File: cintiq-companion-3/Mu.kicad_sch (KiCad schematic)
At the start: 12 parts, among them J1 Conn_01x03_Pin

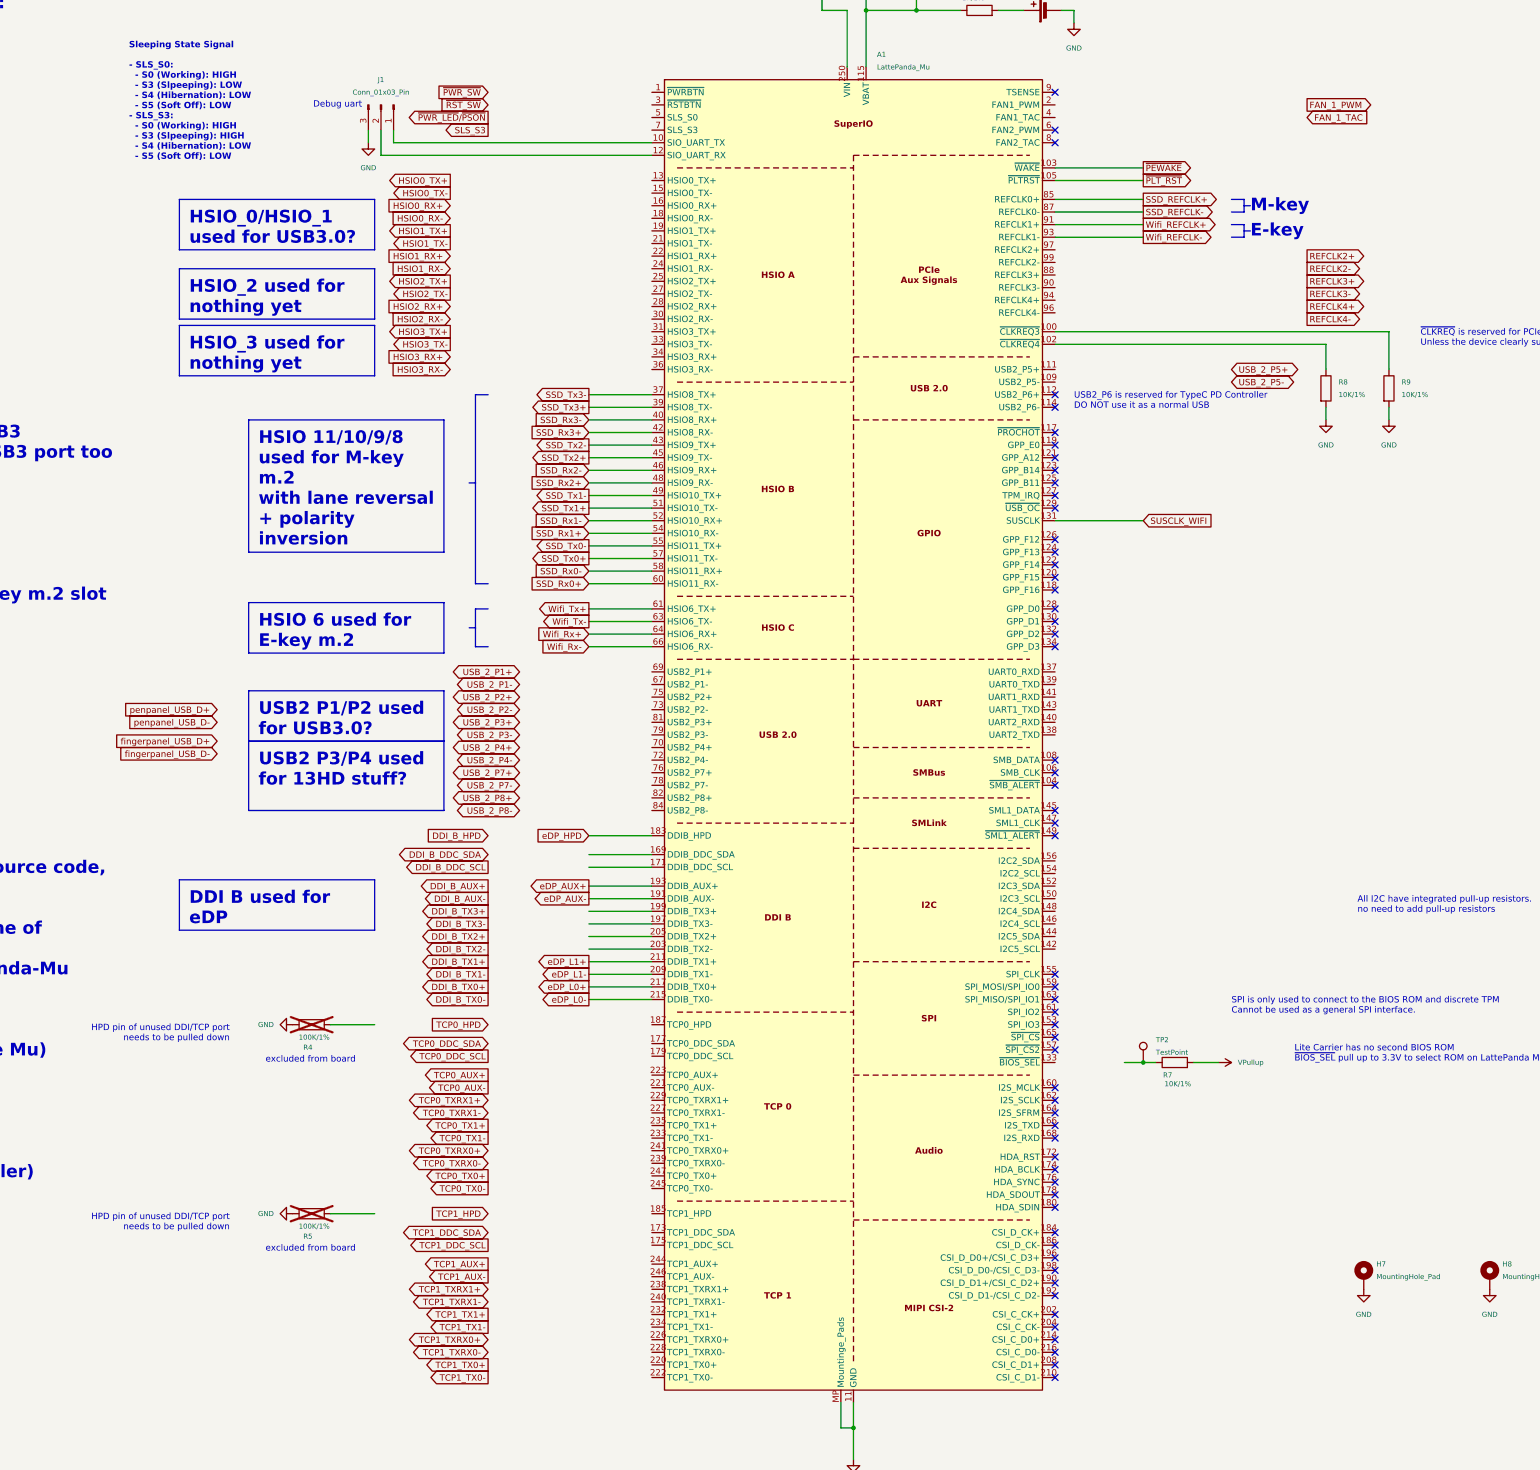
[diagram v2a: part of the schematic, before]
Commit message: routed usb
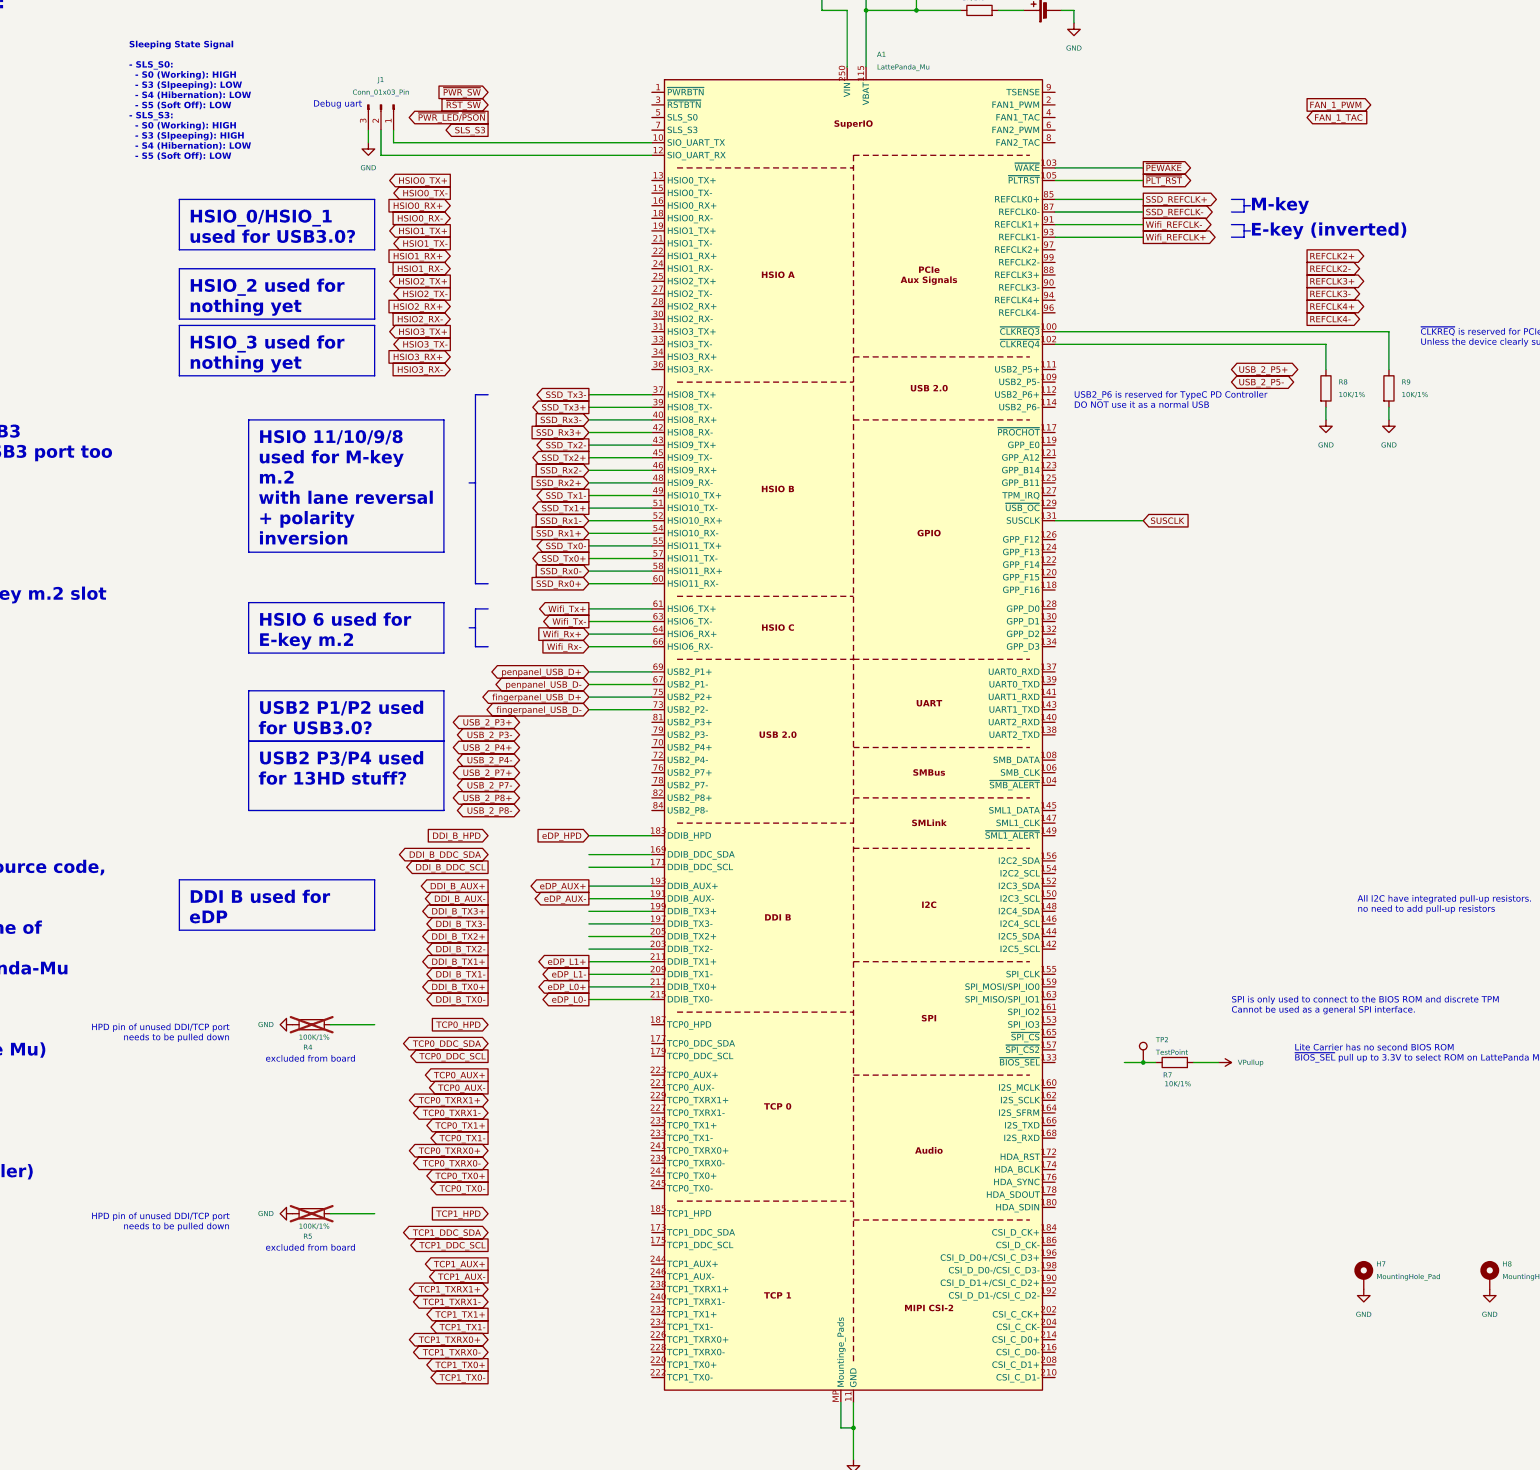
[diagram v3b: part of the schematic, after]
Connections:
- net Wifi_REFCLK+: now also A1.93 (REFCLK1-); no longer A1.91 (REFCLK1+)
- net Wifi_REFCLK-: now also A1.91 (REFCLK1+); no longer A1.93 (REFCLK1-)
- net fingerpanel_USB_D+: now also A1.75 (USB2_P2+)
- net fingerpanel_USB_D-: now also A1.73 (USB2_P2-)
- net penpanel_USB_D+: now also A1.69 (USB2_P1+)
- net penpanel_USB_D-: now also A1.67 (USB2_P1-)
- net SUSCLK_WIFI renamed SUSCLK
- no-connect marks 56 -> 0
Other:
- note added: "E-key (inverted)"
- note removed: "E-key"

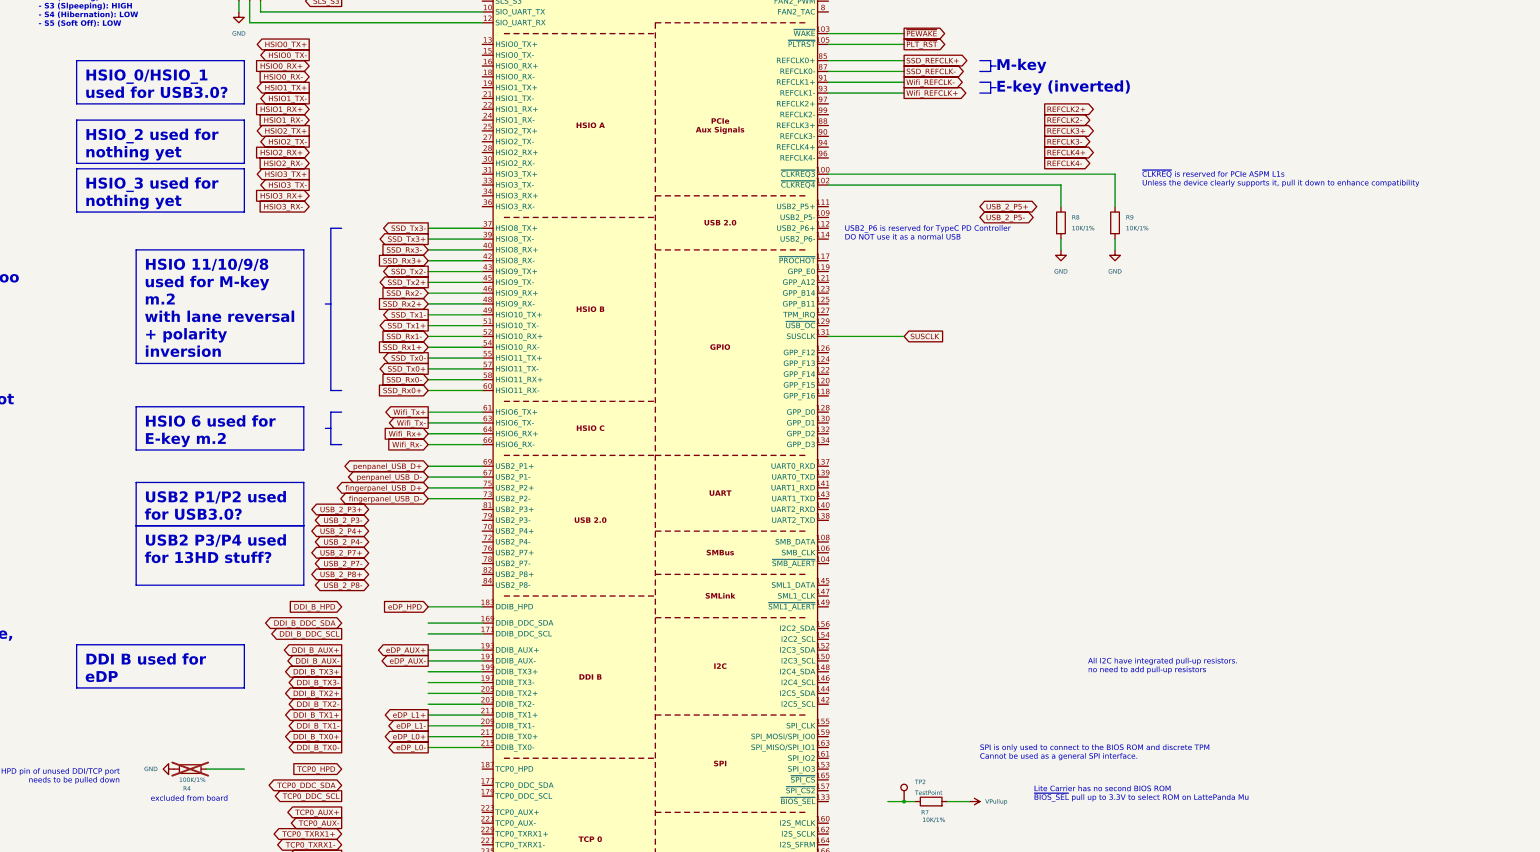
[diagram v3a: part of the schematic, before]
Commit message: Added B-key slot and dual bios chips
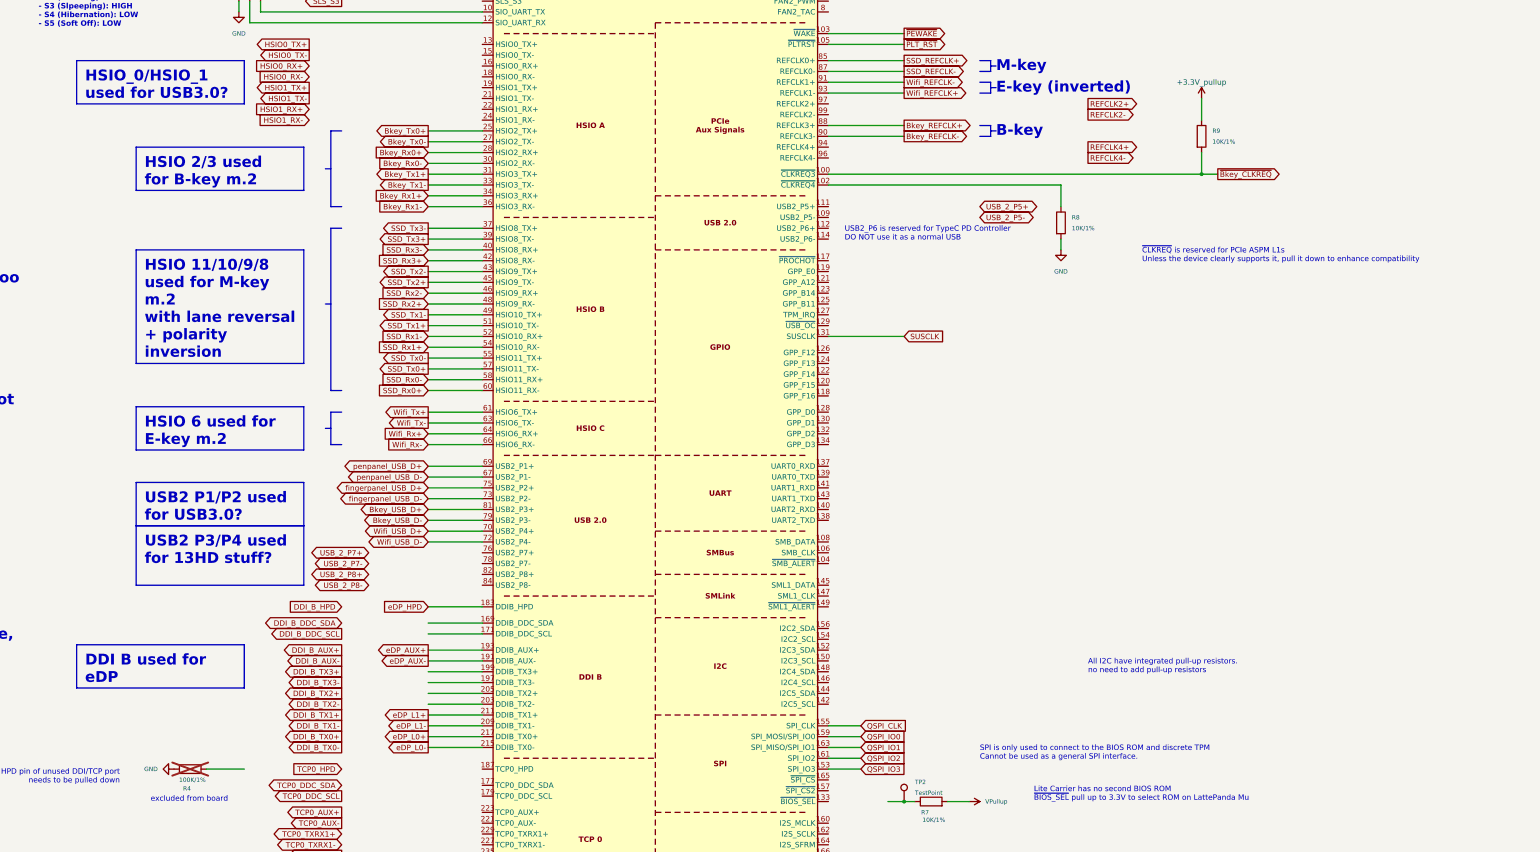
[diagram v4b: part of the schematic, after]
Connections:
- net GND: no longer R9.2
- net +3.3V_pullup: now reaches R9.1
- net +3.3V_pullup: no longer A1.100 (~{CLKREQ3})
- net QSPI_IO3: now reaches A1.153 (SPI_IO3)
- net QSPI_CLK: now reaches A1.155 (SPI_CLK)
- net QSPI_IO0: now reaches A1.159 (SPI_MOSI/SPI_IO0)
- net QSPI_IO2: now reaches A1.161 (SPI_IO2)
- net QSPI_IO1: now reaches A1.163 (SPI_MISO/SPI_IO1)
- net Bkey_Tx0+: now reaches A1.25 (HSIO2_TX+)
- net Bkey_Tx0-: now reaches A1.27 (HSIO2_TX-)
- net Bkey_Rx0+: now reaches A1.28 (HSIO2_RX+)
- net Bkey_Rx0-: now reaches A1.30 (HSIO2_RX-)
- net Bkey_Tx1+: now reaches A1.31 (HSIO3_TX+)
- net Bkey_Tx1-: now reaches A1.33 (HSIO3_TX-)
- net Bkey_Rx1+: now reaches A1.34 (HSIO3_RX+)
- net Bkey_Rx1-: now reaches A1.36 (HSIO3_RX-)
- net Wifi_USB_D+: now reaches A1.70 (USB2_P4+)
- net Wifi_USB_D-: now reaches A1.72 (USB2_P4-)
- net Bkey_USB_D-: now reaches A1.79 (USB2_P3-)
- net Bkey_USB_D+: now reaches A1.81 (USB2_P3+)
- net Bkey_REFCLK+: now reaches A1.88 (REFCLK3+)
- net Bkey_REFCLK-: now reaches A1.90 (REFCLK3-)
- new net ~{Bkey_CLKREQ}: A1.100 (~{CLKREQ3}), R9.2
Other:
- note added: "B-key"
- moved on the sheet: R9

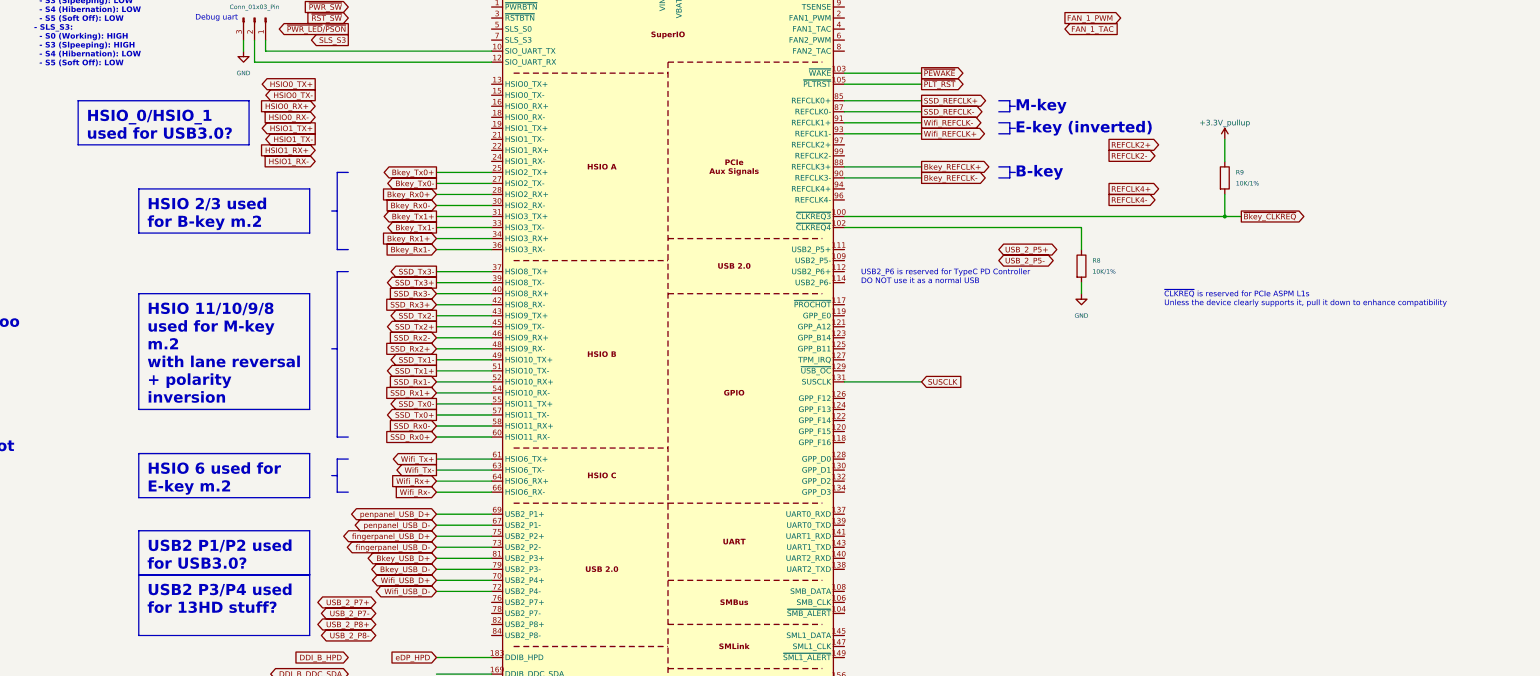
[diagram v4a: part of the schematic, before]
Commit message: Added USB3 and 2nd E-key link
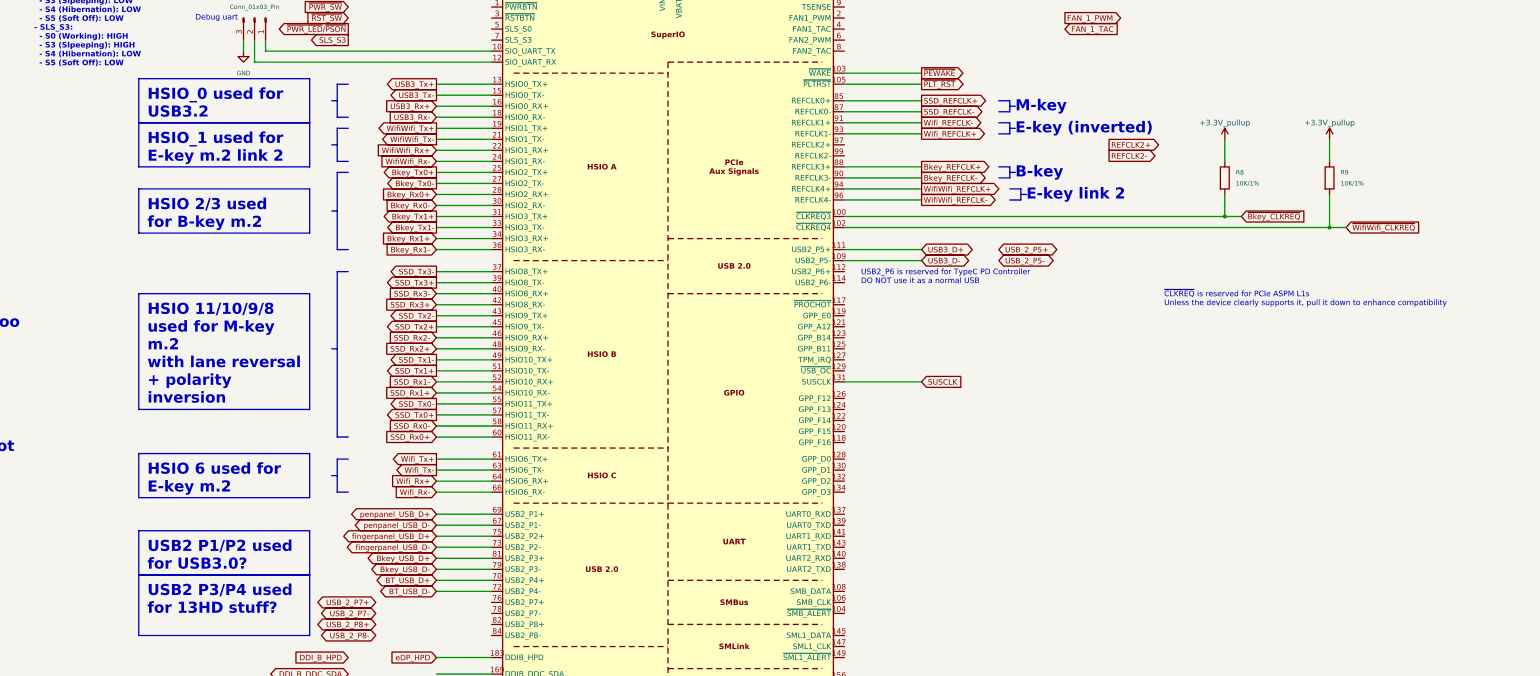
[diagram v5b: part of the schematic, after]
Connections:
- net +3.3V_pullup: now also R8.1
- net GND: no longer R8.2
- net ~{Bkey_CLKREQ}: now also R8.2; no longer R9.2
- net ~{WifiWifi_CLKREQ}: now reaches A1.102 (~{CLKREQ4})
- net ~{WifiWifi_CLKREQ}: now also R9.2; no longer R8.1
- net USB3_D-: now reaches A1.109 (USB2_P5-)
- net USB3_D+: now reaches A1.111 (USB2_P5+)
- net USB3_Tx+: now reaches A1.13 (HSIO0_TX+)
- net USB3_Tx-: now reaches A1.15 (HSIO0_TX-)
- net USB3_Rx+: now reaches A1.16 (HSIO0_RX+)
- net USB3_Rx-: now reaches A1.18 (HSIO0_RX-)
- net WifiWifi_Tx+: now reaches A1.19 (HSIO1_TX+)
- net WifiWifi_Tx-: now reaches A1.21 (HSIO1_TX-)
- net WifiWifi_Rx+: now reaches A1.22 (HSIO1_RX+)
- net WifiWifi_Rx-: now reaches A1.24 (HSIO1_RX-)
- net WifiWifi_REFCLK+: now reaches A1.94 (REFCLK4+)
- net WifiWifi_REFCLK-: now reaches A1.96 (REFCLK4-)
- net Wifi_USB_D+ renamed BT_USB_D+
- net Wifi_USB_D- renamed BT_USB_D-
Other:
- note added: "E-key link 2"
- moved on the sheet: R8, R9
